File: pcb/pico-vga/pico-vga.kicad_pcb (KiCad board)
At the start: 2 copper layers, 85 x 110 mm, 71 parts, among them J1 DB15_Female_HighDensity, J2 Micro_SD_Card, J3 AudioJack3, J4 USB_C_Receptacle, J5 USB_C_Receptacle, J6 USB_C_Receptacle, J7 USB_C_Receptacle, J8 Conn_01x05_Male, J9 Conn_01x02_Male, SW1 SW_Push, U1 Raspberry_Pi_Pico, U10 SN74LVC08A, U11 SN74LVC08A, U12 SN74LVC08A, U13 CD4072B, U14 CD4072B, U15 CD4072B, U16 CD4072B, U2 74LVC2G34, U3 74LVC04A, U4 SN74LVC139A, U5 SN74LVC08A, U6 SN74LVC08A, U7 SN74LVC08A, U8 SN74LVC08A, U9 SN74LVC08A

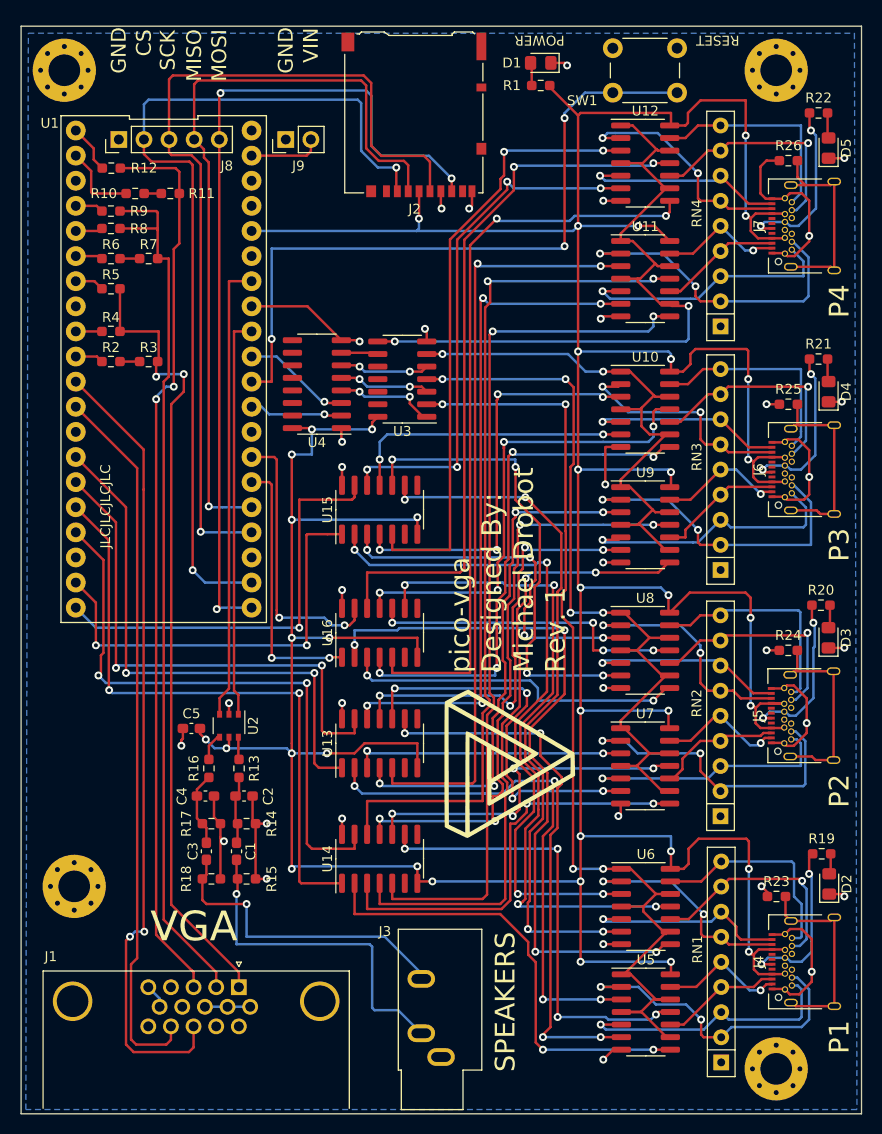
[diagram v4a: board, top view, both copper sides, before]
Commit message: PCB v2 done
This update removed most of the stuff on the board -- the massive controller multiplexer is now replaced with an ATTiny24 on the controller side and an I2C bus. The buffer for the audio circuit is also gone. The board now supports surface mounting the pico, and is significantly smaller.
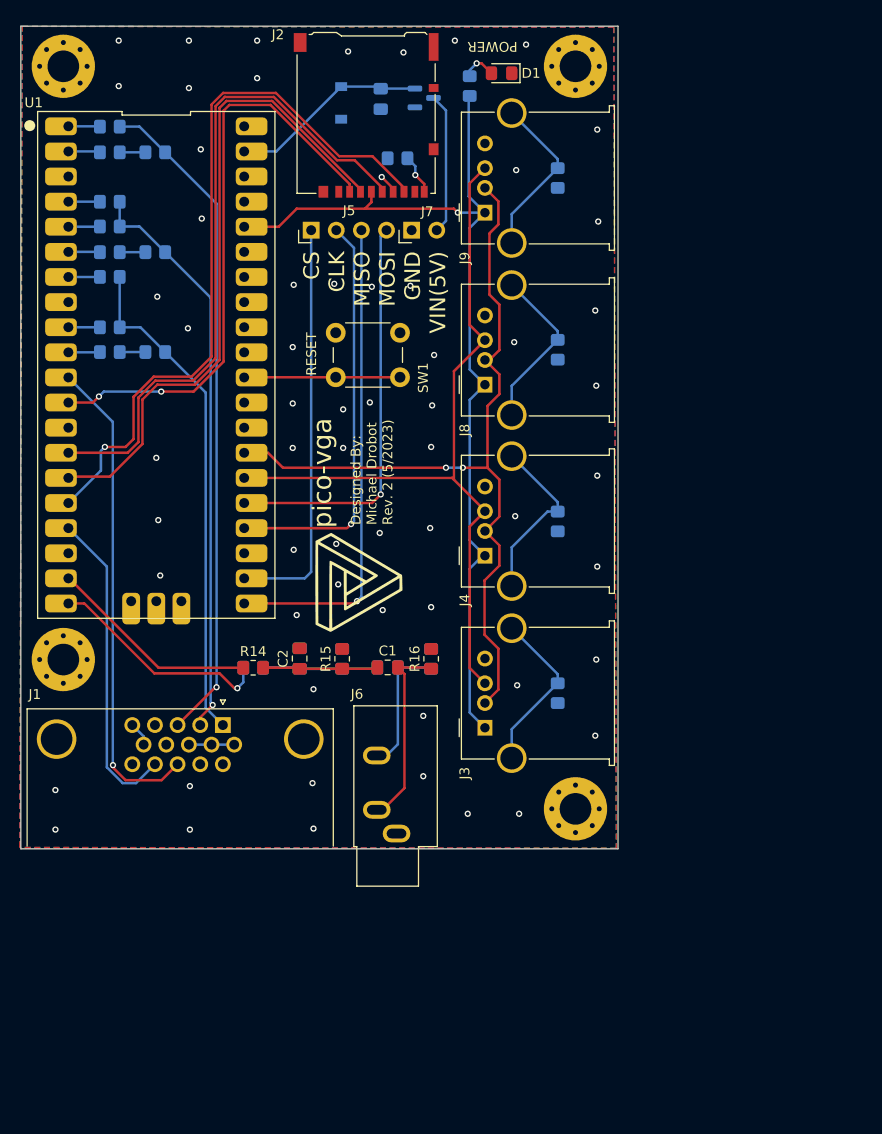
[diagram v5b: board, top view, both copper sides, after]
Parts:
- removed D3, D4, D5: LED, LED_SMD:LED_0805_2012Metric_Pad1.15x1.40mm_HandSolder
- removed the G*** at (64.1, 87.1)
- removed R24, R25, R26: 1M, Resistor_SMD:R_0603_1608Metric_Pad0.98x0.95mm_HandSolder
- removed the REF** at (91.0, 118.0)
- removed the REF** at (19.0, 17.0)
- removed the REF** at (91.0, 17.0)
- removed the REF** at (20.0, 99.5)
- removed RN1, RN2, RN3, RN4: 10K, Resistor_THT:R_Array_SIP9
- removed U10, U11, U12, U5, U6, U7, U8, U9: SN74LVC08A, Package_SO:SOIC-14_3.9x8.7mm_P1.27mm
- removed U13, U14, U15, U16: CD4072B, Package_SO:SOIC-14_3.9x8.7mm_P1.27mm
- removed U2: 74LVC2G34, Package_SO:TSOP-6_1.65x3.05mm_P0.95mm
- removed U3: 74LVC04A, Package_SO:SOIC-14_3.9x8.7mm_P1.27mm
- removed U4: SN74LVC139A, Package_SO:SOIC-16_3.9x9.9mm_P1.27mm
- added G***: LOGO, LOGO, F.Cu at (48.8, 68.8)
- added Q1: DMP3099L-7, Package_TO_SOT_SMD:SOT-23, B.Cu at (55.4, 19.8)
- added REF**: MountingHole_3.2mm_M3_Pad_Via, MountingHole:MountingHole_3.2mm_M3_Pad_Via, F.Cu at (70.7, 91.7)
- added REF**: MountingHole_3.2mm_M3_Pad_Via, MountingHole:MountingHole_3.2mm_M3_Pad_Via, F.Cu at (70.7, 16.6)
- added REF**: MountingHole_3.2mm_M3_Pad_Via, MountingHole:MountingHole_3.2mm_M3_Pad_Via, F.Cu at (18.9, 16.6)
- added REF**: MountingHole_3.2mm_M3_Pad_Via, MountingHole:MountingHole_3.2mm_M3_Pad_Via, F.Cu at (18.9, 76.6)
- C1, C2: footprint Capacitor_SMD:C_0603_1608Metric_Pad1.08x0.95mm_HandSolder -> Capacitor_SMD:C_0805_2012Metric_Pad1.18x1.45mm_HandSolder
- C3, C4: footprint Capacitor_SMD:C_0603_1608Metric_Pad1.08x0.95mm_HandSolder -> Capacitor_SMD:C_0805_2012Metric_Pad1.18x1.45mm_HandSolder; moved to B.Cu
- C5: value 100n -> 47u; footprint Capacitor_SMD:C_0603_1608Metric_Pad1.08x0.95mm_HandSolder -> Capacitor_SMD:C_0805_2012Metric_Pad1.18x1.45mm_HandSolder; moved to B.Cu
- D2: value LED -> MMSZ5233BT1G; footprint LED_SMD:LED_0805_2012Metric_Pad1.15x1.40mm_HandSolder -> Diode_SMD:D_SOD-123; moved to B.Cu
- J3: value AudioJack3 -> USB_A; footprint Connector_Audio:Jack_3.5mm_CUI_SJ1-3533NG_Horizontal -> Connector_USB:USB_A_Molex_67643_Horizontal
- J4: value USB_C_Receptacle -> USB_A; footprint pico-vga:USB_C_Receptacle_Molex_2171830001 -> Connector_USB:USB_A_Molex_67643_Horizontal
- J5: value USB_C_Receptacle -> Conn_01x04_Male; footprint pico-vga:USB_C_Receptacle_Molex_2171830001 -> Connector_PinHeader_2.54mm:PinHeader_1x04_P2.54mm_Horizontal
- J6: value USB_C_Receptacle -> AudioJack3; footprint pico-vga:USB_C_Receptacle_Molex_2171830001 -> Connector_Audio:Jack_3.5mm_CUI_SJ1-3533NG_Horizontal
- J7: value USB_C_Receptacle -> Conn_01x02_Male; footprint pico-vga:USB_C_Receptacle_Molex_2171830001 -> Connector_PinHeader_2.54mm:PinHeader_1x02_P2.54mm_Horizontal
- J8: value Conn_01x05_Male -> USB_A; footprint Connector_PinHeader_2.54mm:PinHeader_1x05_P2.54mm_Vertical -> Connector_USB:USB_A_Molex_67643_Horizontal
- J9: value Conn_01x02_Male -> USB_A; footprint Connector_PinHeader_2.54mm:PinHeader_1x02_P2.54mm_Vertical -> Connector_USB:USB_A_Molex_67643_Horizontal
- R1, R10, R11, R12, R2, R23, R3, R4, R5, R6, R7, R8, R9: footprint Resistor_SMD:R_0603_1608Metric_Pad0.98x0.95mm_HandSolder -> Resistor_SMD:R_0805_2012Metric_Pad1.20x1.40mm_HandSolder; moved to B.Cu
- R13: value 220 -> 1M; footprint Resistor_SMD:R_0603_1608Metric_Pad0.98x0.95mm_HandSolder -> Resistor_SMD:R_0805_2012Metric_Pad1.20x1.40mm_HandSolder; moved to B.Cu
- R14: value 100 -> 220; footprint Resistor_SMD:R_0603_1608Metric_Pad0.98x0.95mm_HandSolder -> Resistor_SMD:R_0805_2012Metric_Pad1.20x1.40mm_HandSolder
- R15: value 1.8K -> 100; footprint Resistor_SMD:R_0603_1608Metric_Pad0.98x0.95mm_HandSolder -> Resistor_SMD:R_0805_2012Metric_Pad1.20x1.40mm_HandSolder
- R16: value 220 -> 1.8K; footprint Resistor_SMD:R_0603_1608Metric_Pad0.98x0.95mm_HandSolder -> Resistor_SMD:R_0805_2012Metric_Pad1.20x1.40mm_HandSolder
- R17: value 100 -> 1M; footprint Resistor_SMD:R_0603_1608Metric_Pad0.98x0.95mm_HandSolder -> Resistor_SMD:R_0805_2012Metric_Pad1.20x1.40mm_HandSolder; moved to B.Cu
- R18: value 1.8K -> 1M; footprint Resistor_SMD:R_0603_1608Metric_Pad0.98x0.95mm_HandSolder -> Resistor_SMD:R_0805_2012Metric_Pad1.20x1.40mm_HandSolder; moved to B.Cu
- R19: value 1K -> 220; footprint Resistor_SMD:R_0603_1608Metric_Pad0.98x0.95mm_HandSolder -> Resistor_SMD:R_0805_2012Metric_Pad1.20x1.40mm_HandSolder; moved to B.Cu
- R20: value 1K -> 100; footprint Resistor_SMD:R_0603_1608Metric_Pad0.98x0.95mm_HandSolder -> Resistor_SMD:R_0805_2012Metric_Pad1.20x1.40mm_HandSolder; moved to B.Cu
- R21: value 1K -> 1.8K; footprint Resistor_SMD:R_0603_1608Metric_Pad0.98x0.95mm_HandSolder -> Resistor_SMD:R_0805_2012Metric_Pad1.20x1.40mm_HandSolder; moved to B.Cu
- R22: value 1K -> 1M; footprint Resistor_SMD:R_0603_1608Metric_Pad0.98x0.95mm_HandSolder -> Resistor_SMD:R_0805_2012Metric_Pad1.20x1.40mm_HandSolder; moved to B.Cu
- moved D2 93.1 mm to (47.0, 20.3), turned to -90 degrees
- moved R23 76.0 mm to (68.9, 27.9), turned to 90 degrees
- moved J5 71.2 mm to (44.0, 33.2)
- moved C5 66.5 mm to (51.0, 19.9), turned to 90 degrees
- moved R13 63.8 mm to (52.7, 25.9), turned to 180 degrees
- moved R19 60.5 mm to (38.1, 77.4), turned to 0 degrees
- moved J6 56.6 mm to (52.6, 94.2), turned to 180 degrees
- moved J4 53.4 mm to (61.5, 66.1)
- moved R18 50.3 mm to (68.9, 62.6), turned to 90 degrees
- moved R21 49.5 mm to (56.1, 76.5), turned to 90 degrees
- moved R20 48.7 mm to (47.1, 76.5), turned to 90 degrees
- moved J8 44.6 mm to (61.5, 48.8)
- moved J7 41.5 mm to (54.1, 33.2)
- moved SW1 40.2 mm to (53.0, 48.0)
- moved R17 37.4 mm to (68.9, 80.0), turned to 90 degrees
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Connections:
- C5 pad 1: +3V3 -> GND
- C5 pad 2: GND -> +5V
- D2 pad 1: GND -> +5V
- D2 pad 2: Net-(D2-Pad2) -> GND
- J2 pad 9: GND -> Net-(J2-Pad9)
- J8 pad 1: GND -> +3V3
- J8 pad 2: /SD_CS -> /CONTROLLER_SCL
- J8 pad 3: /SD_CLK -> /CONTROLLER_SDA
- J8 pad 4: /SD_MOSI -> GND
- J8 pad 5: /SD_MISO -> Net-(J8-Pad5)
- J9 pad 1: GND -> +3V3
- J9 pad 2: +5V -> /CONTROLLER_SCL
- R13 pad 1: Net-(R13-Pad1) -> Net-(J2-Pad9)
- R13 pad 2: Net-(C1-Pad1) -> GND
- R14 pad 1: Net-(C1-Pad1) -> /AUDIO_L
- R14 pad 2: GND -> Net-(C1-Pad1)
- R15 pad 1: Net-(C1-Pad2) -> Net-(C1-Pad1)
- R16 pad 1: Net-(R16-Pad1) -> Net-(C1-Pad2)
- R16 pad 2: Net-(C3-Pad1) -> GND
- R17 pad 1: Net-(C3-Pad1) -> GND
- R17 pad 2: GND -> Net-(J3-Pad5)
- R18 pad 1: Net-(C3-Pad2) -> GND
- R18 pad 2: GND -> Net-(J4-Pad5)
- R19 pad 1: Net-(D2-Pad2) -> /AUDIO_R
- R19 pad 2: Net-(J4-PadA6) -> Net-(C3-Pad1)
- R20 pad 1: Net-(D3-Pad2) -> Net-(C3-Pad1)
- R20 pad 2: Net-(J5-PadA6) -> GND
- R21 pad 1: Net-(D4-Pad2) -> Net-(C3-Pad2)
- R21 pad 2: Net-(J6-PadA6) -> GND
- R22 pad 1: Net-(D5-Pad2) -> GND
- R22 pad 2: Net-(J7-PadA6) -> Net-(J8-Pad5)
- R23 pad 1: Net-(J4-PadS1) -> GND
- R23 pad 2: GND -> Net-(J9-Pad5)
- U1 pad 12: /VSYNC -> /SD_CS
- U1 pad 14: DPAD_UP -> /SD_CLK
- U1 pad 15: DPAD_DOWN -> /SD_MOSI
- U1 pad 16: DPAD_LEFT -> /SD_MISO
- U1 pad 17: DPAD_RIGHT -> /VSYNC
- U1 pad 19: BTN_A -> /AUDIO_L
- U1 pad 20: BTN_B -> /AUDIO_R
- U1 pad 21: /SD_MISO -> /PERIPHERAL_MISO
- U1 pad 22: /SD_CS -> /PERIPHERAL_CS
- U1 pad 24: /SD_CLK -> /PERIPHERAL_CLK
- U1 pad 25: /SD_MOSI -> /PERIPHERAL_MOSI
- U1 pad 26: BTN_X -> /CONTROLLER_SDA
- U1 pad 27: BTN_Y -> /CONTROLLER_SCL
- U1 pad 29: CONTROLLER_SEL_A -> unconnected-(U1-Pad29)
- U1 pad 31: CONTROLLER_SEL_B -> unconnected-(U1-Pad31)
- U1 pad 32: /AUDIO_L -> unconnected-(U1-Pad32)
- U1 pad 34: /AUDIO_R -> unconnected-(U1-Pad34)
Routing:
- net +3V3: track 478.9 -> 95.8 mm, vias 38 -> 1
- net GND: track 143.5 -> 9.00 mm, vias 34 -> 62
- net /ControllerInterface/CONTROLLER_SEL_1: track 104.5 -> 0.00 mm, vias 4 -> 0
- net /ControllerInterface/C4_DPAD_LEFT: track 88.0 -> 0.00 mm, vias 2 -> 0
- net /ControllerInterface/C4_DPAD_RIGHT: track 86.9 -> 0.00 mm, vias 2 -> 0
- net /CONTROLLER_SCL: track 0.00 -> 84.1 mm, vias 0 -> 2
- net /CONTROLLER_SDA: track 0.00 -> 78.5 mm
- net /ControllerInterface/CONTROLLER_SEL_2: track 78.4 -> 0.00 mm, vias 4 -> 0
- net /ControllerInterface/C4_DPAD_UP: track 77.1 -> 0.00 mm, vias 2 -> 0
- net /ControllerInterface/C4_BTN_X: track 75.6 -> 0.00 mm, vias 2 -> 0
- net /ControllerInterface/C1_BTN_X: track 73.4 -> 0.00 mm, vias 4 -> 0
- net /ControllerInterface/CONTROLLER_SEL_4: track 73.3 -> 0.00 mm, vias 2 -> 0
- net /ControllerInterface/C4_BTN_Y: track 72.2 -> 0.00 mm, vias 2 -> 0
- net /ControllerInterface/C1_BTN_B: track 71.5 -> 0.00 mm, vias 4 -> 0
- net /ControllerInterface/C1_BTN_A: track 68.8 -> 0.00 mm, vias 4 -> 0
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- added copper zone on F.Cu, net GND
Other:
- board size 85 x 110 mm -> 60.4 x 83.2 mm
- board text added: "CS CLK MISO MOSI GND VIN(5V)"
- board text added: "Designed By: Michael Drobot Rev. 2 (5/2023)"
- board text added: "pico-vga"
- board text removed: "CS"
- board text removed: "GND"
- board text removed: "JLCJLCJLCJLC"
- board text removed: "MISO"
- board text removed: "MOSI"
- board text removed: "P1"
- board text removed: "P2"
- board text removed: "P3"
- board text removed: "P4"
- board text removed: "SCK"
- board text removed: "SPEAKERS"
- board text removed: "VGA"
- board text removed: "VIN"
- board text removed: "VIN: 1.8-5.5VDC"
- board text removed: "pico-vga Designed By: Michael Drobot Rev. 1"

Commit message: PCB update and BOM
Remade the BOM so now you can just export to csv and throw it into digikey, makes it a lot easier. In making the BOM I realized some of my old parts were super expensive, so I redid some components
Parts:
- J2: value Micro_SD_Card -> Micro_SD_Card_Det; footprint Connector_Card:microSD_HC_Hirose_DM3AT-SF-PEJM5 -> pico-vga:MEM2061-01-188-00-A_GCT
- J6: footprint Connector_Audio:Jack_3.5mm_CUI_SJ1-3533NG_Horizontal -> pico-vga:STX-3000_KYC
- R13: moved to F.Cu
- moved R13 17.0 mm to (38.5, 16.5)
- moved J6 6.96 mm to (53.4, 87.3)
- moved D2 5.41 mm to (45.9, 25.6)
- moved C5 5.18 mm to (50.1, 25.0)
- moved Q1 5.10 mm to (55.2, 24.9)
- moved J2 0.81 mm to (49.8, 20.8)
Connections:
- J2 pad 10: (no net) -> unconnected-(J2-Pad10)
- J2 pad 11: (no net) -> Net-(R13-Pad1)
- J2 pad 9: Net-(J2-Pad9) -> unconnected-(J2-Pad9)
- R13 pad 1: Net-(J2-Pad9) -> Net-(R13-Pad1)
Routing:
- net Net-(R13-Pad1): track 0.00 -> 18.3 mm
- net +3V3: track 95.8 -> 104.1 mm, vias 1 -> 2
- net Net-(C1-Pad2): track 19.6 -> 13.4 mm
- net Net-(J7-Pad2): track 14.3 -> 8.49 mm
- net /SD_MISO: track 74.1 -> 68.7 mm, vias 1 -> 0
- net Net-(J2-Pad9): track 4.10 -> 0.00 mm, vias 1 -> 0
- net Net-(C3-Pad2): track 13.8 -> 9.70 mm
- net /SD_MOSI: track 66.9 -> 63.1 mm
- net /SD_CLK: track 68.4 -> 64.7 mm, vias 0 -> 2
- net /SD_CS: track 59.9 -> 57.2 mm, vias 2 -> 0
- net +5V: track 20.1 -> 17.6 mm
- net GND: track 9.00 -> 7.03 mm, vias 62 -> 67
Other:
- board size 60.4 x 83.2 mm -> 60.4 x 83.3 mm

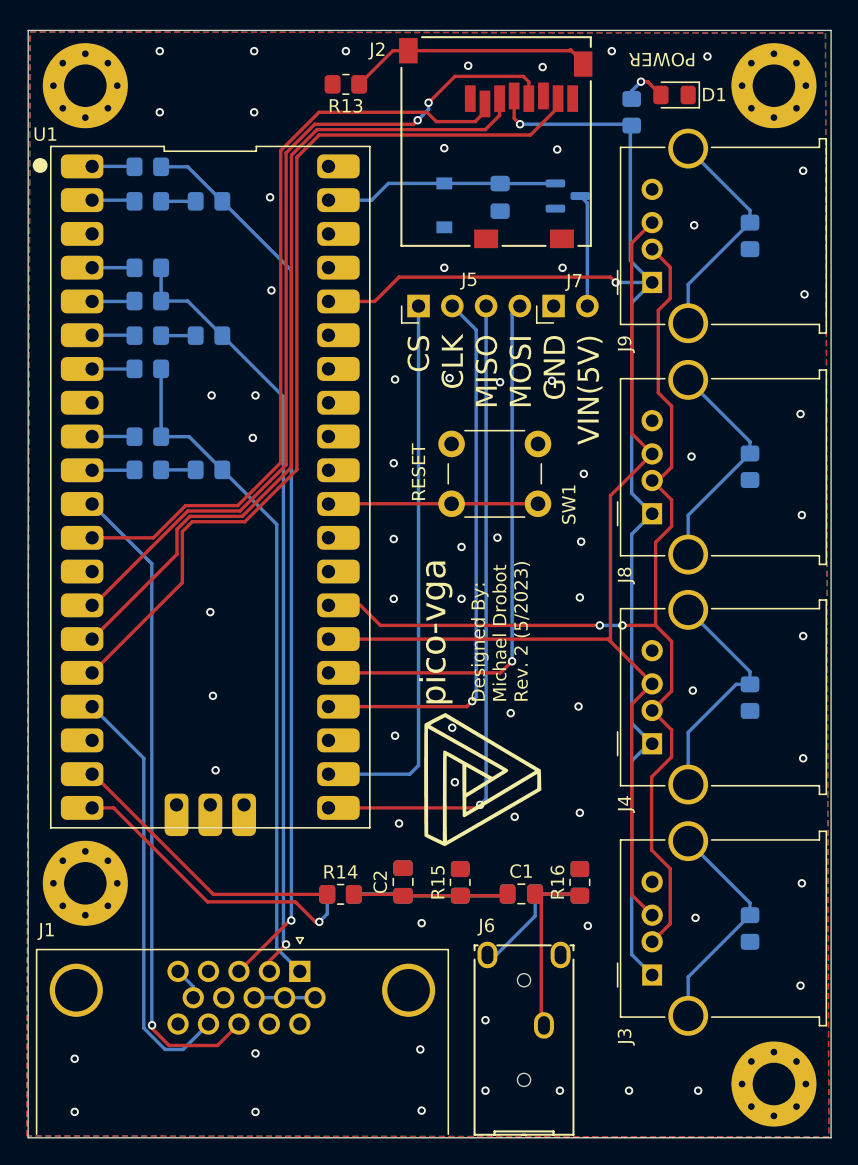
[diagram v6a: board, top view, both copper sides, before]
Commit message: pico-vga PCB rev. 3
 - Added proper protections for external pins this time
 - Denser layout, smaller overall footprint
 - Swapped to 4 layer for hopefully better EMI performance
 - Tried to do layout optimized for limiting crosstalk, especially on VGA/audio/sd card SPI lines
 - After much indecision, going forward with I2C controller support
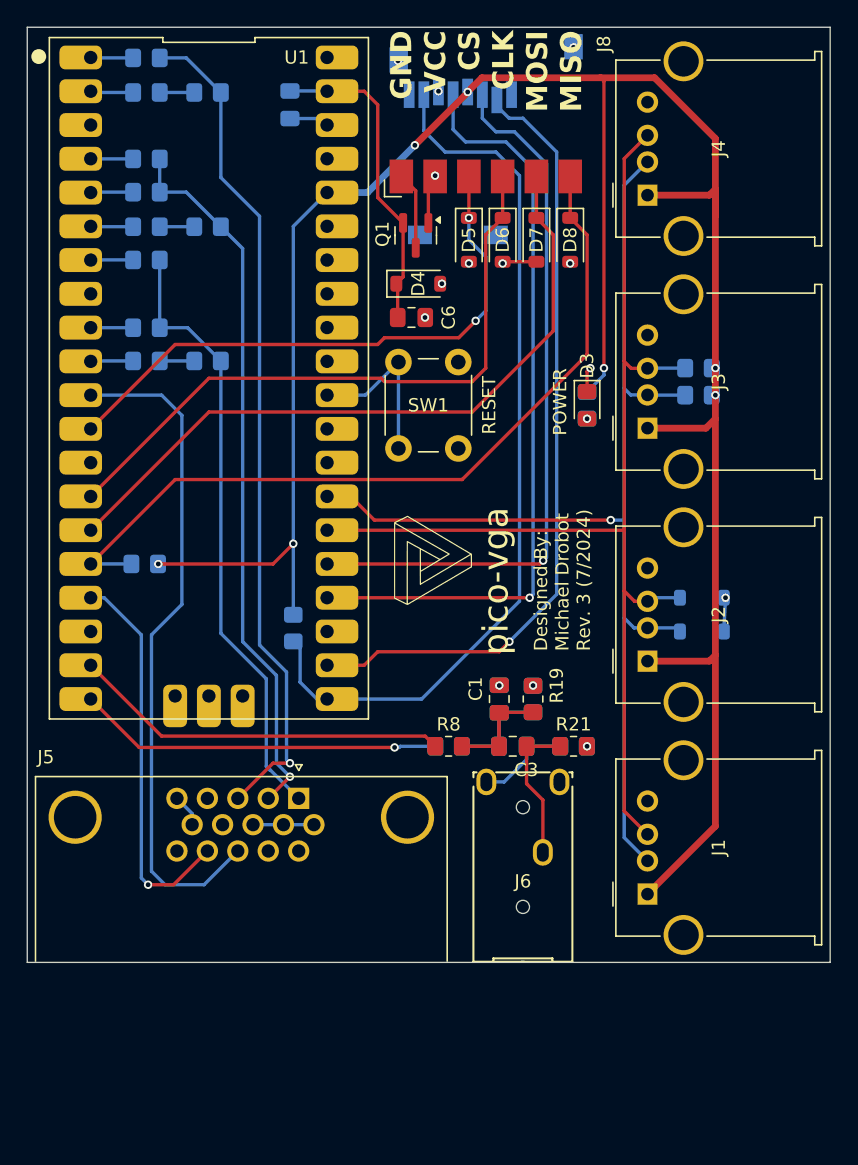
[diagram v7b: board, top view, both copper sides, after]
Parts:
- removed the J5 at (44.0, 33.2)
- removed the J7 at (54.1, 33.2)
- removed the R13 at (38.5, 16.5)
- removed the R17 at (68.9, 80.0)
- removed the R18 at (68.9, 62.6)
- removed the R22 at (68.9, 45.3)
- removed R23: 1M, Resistor_SMD:R_0805_2012Metric_Pad1.20x1.40mm_HandSolder
- removed REF** (x4): MountingHole_3.2mm_M3_Pad_Via, MountingHole:MountingHole_3.2mm_M3_Pad_Via
- added C5: 100n, Capacitor_SMD:C_0805_2012Metric_Pad1.18x1.45mm_HandSolder, B.Cu at (34.3, 18.0)
- added D1: 3.6V, Diode_SMD:D_SOD-123, B.Cu at (65.3, 55.1)
- added D2: 3.6V, Diode_SMD:D_SOD-123, B.Cu at (65.3, 57.7)
- added D5: 3.6V, Diode_SMD:D_SOD-123, F.Cu at (47.8, 28.2)
- added D6: 3.6V, Diode_SMD:D_SOD-123, F.Cu at (50.3, 28.2)
- added D7: 3.6V, Diode_SMD:D_SOD-123, F.Cu at (52.8, 28.2)
- added D8: 3.6V, Diode_SMD:D_SOD-123, F.Cu at (55.4, 28.2)
- added J8: Conn_01x06_Pin, pico-vga:PinHeader_1x06_P2.54mm_Horizontal_SMD, F.Cu at (42.7, 23.4)
- added R1: 4.7K, Resistor_SMD:R_0805_2012Metric_Pad1.20x1.40mm_HandSolder, B.Cu at (23.4, 52.6)
- added R2: 4.7K, Resistor_SMD:R_0805_2012Metric_Pad1.20x1.40mm_HandSolder, B.Cu at (65.0, 39.9)
- added R3: 4.7K, Resistor_SMD:R_0805_2012Metric_Pad1.20x1.40mm_HandSolder, B.Cu at (65.0, 37.8)
- added R4: 4.7K, Resistor_SMD:R_0805_2012Metric_Pad1.20x1.40mm_HandSolder, B.Cu at (34.5, 57.4)
- C6: renamed from C5; value 47u -> 10u; moved to F.Cu
- D4: renamed from D2; value MMSZ5233BT1G -> 5.1V; moved to F.Cu
- G***: footprint LOGO -> pico-vga:Logo
- J7: renamed from J2; moved to B.Cu
- Q1: moved to F.Cu
- moved D3 24.3 mm to (56.6, 40.6), turned to -90 degrees
- moved J3 23.7 mm to (61.2, 42.4)
- moved R5 22.3 mm to (56.6, 40.6), turned to -90 degrees
- moved G*** 16.9 mm to (45.0, 52.3)
- moved C1 15.5 mm to (50.0, 62.7)
- moved C2 15.5 mm to (50.0, 62.7)
- moved R19 14.8 mm to (52.6, 62.7)
- moved R20 14.8 mm to (52.6, 62.7)
- moved R8 13.8 mm to (46.2, 66.3)
- moved R9 13.8 mm to (46.2, 66.3)
- moved J5 13.0 mm to (35.0, 70.2)
- moved J6 13.0 mm to (53.3, 74.3)
- moved Q1 11.8 mm to (43.8, 27.9), turned to -90 degrees
- moved SW1 11.3 mm to (42.5, 43.9), turned to 90 degrees
- moved C6 11.2 mm to (43.4, 34.0), turned to 180 degrees
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- renumbered C2 to C1, C4 to C2, C1 to C3, C3 to C4, D1 to D3, J3 to J1, J8 to J2, J4 to J3, J9 to J4, J1 to J5, R4 to R10, R8 to R11, R2 to R13, R6 to R14, R10 to R15, R3 to R16, R7 to R17, R11 to R18, R15 to R19, R16 to R21, R21 to R22, R1 to R5, R5 to R6, R9 to R7, R14 to R8, R19 to R9
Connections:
- J1 pad 5: Net-(J3-Pad5) -> GND
- J2 pad 5: Net-(J8-Pad5) -> GND
- J3 pad 5: Net-(J4-Pad5) -> GND
- J4 pad 5: Net-(J9-Pad5) -> GND
- J7 pad 11: Net-(R13-Pad1) -> GND
- U1 pad 12: /SD_CS -> /PERIPHERAL_CS
- U1 pad 14: /SD_CLK -> /PERIPHERAL_CLK
- U1 pad 15: /SD_MOSI -> /PERIPHERAL_MOSI
- U1 pad 16: /SD_MISO -> /PERIPHERAL_MISO
- U1 pad 21: /PERIPHERAL_MISO -> /SD_MISO
- U1 pad 22: /PERIPHERAL_CS -> /SD_CS
- U1 pad 24: /PERIPHERAL_CLK -> /SD_CLK
- U1 pad 25: /PERIPHERAL_MOSI -> /SD_MOSI
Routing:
- net +3V3: track 104.1 -> 179.6 mm, vias 2 -> 7
- net Net-(R13-Pad1): track 18.3 -> 0.00 mm
- net Net-(J4-Pad5): track 17.6 -> 0.00 mm
- net Net-(J9-Pad5): track 17.0 -> 0.00 mm
- net Net-(J8-Pad5): track 17.0 -> 0.00 mm
- net Net-(J3-Pad5): track 17.0 -> 0.00 mm
- net GND: track 7.03 -> 19.2 mm, vias 67 -> 14
- net /PERIPHERAL_MOSI: track 41.1 -> 53.2 mm, vias 1 -> 0
- net /PERIPHERAL_MISO: track 49.2 -> 60.9 mm, vias 1 -> 0
- net /SD_MOSI: track 63.1 -> 54.3 mm, vias 0 -> 1
- net /PERIPHERAL_CLK: track 41.6 -> 48.9 mm, vias 1 -> 0
- net /SD_CLK: track 64.7 -> 57.5 mm, vias 2 -> 1
- net /AUDIO_L: track 21.4 -> 28.4 mm
- net /CONTROLLER_SDA: track 78.5 -> 85.4 mm
- net +5V: track 17.6 -> 23.4 mm
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- added copper zone on In1.Cu, net GND
- added copper zone on In2.Cu, net GND
- removed copper zone on B.Cu, net GND
- removed copper zone on F.Cu, net GND
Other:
- board size 60.4 x 83.3 mm -> 60.4 x 70.3 mm
- copper layers 2 -> 4
- board text added: "Designed By: Michael Drobot Rev. 3 (7/2024)"
- board text added: "GND VCC CS CLK MOSI MISO"
- board text removed: "CS CLK MISO MOSI GND VIN(5V)"
- board text removed: "Designed By: Michael Drobot Rev. 2 (5/2023)"
